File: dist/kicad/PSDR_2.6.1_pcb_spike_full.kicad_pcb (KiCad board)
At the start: 4 copper layers, 100 x 65 mm, 391 parts, among them J153 0.1in_6P_HEADER_DUAL_ENTRY_12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, J170 SPI_LCD_BOTTOM_ENTRY, M1 MH3M_PLATED, M2 MH3M_PLATED, M3 MH3M_PLATED, M4 MH3M, M5 MH3M, M6 MH3M, M7 MH3M, Q126 MOSFET_P_SOT23_IRLML6401, Q178 MOSFET_P_SOT23_IRLML6401, Q208 MOSFET_P_SOT23_IRLML6401, Q246 MOSFET_P_SOT23_IRLML6401, Q5 MOSFET_P_SOT23_IRLML6401, U114 BUCK_REGULATOR_AP3417C, U121 STM32F746_LQFP100, U131 OP_AMP_FAN4174, U15 DIGITAL_POT_MAX5388, U16 RF_DPDT_MASWSS0129TR, U161 BAT-MANAGE_MCP73871, U172 3V3_LDO_MCP1802, U18 DPDT_ANALOG_MAX4525, U185 GPS_MODULE_RXM-GPS-RM-T, U189 MIC_PREAMP_SSM2167, U199 AUDIO_AMP_TPA0253DGQR, U211 74CBTLV3253, U216 OP_AMP_FAN4174, U227 OP_AMP_FAN4174, U24 RF_DPDT_MASWSS0129TR, U241 SI5338, U253 AD8131, U255 MCP6N11, U260 AD8131, U272 MCP6N11, U279 SY10EP52V, U280 SY10EP52V, U287 VARIABLE_FILTER_HMC1023, U298 74CBTLV3253, U30 RF_DPDT_MASWSS0129TR, U304 MMIC-AMP_HMC482ST, U314 AD8302, U32 MICROPHONE_MEMS_SPU0410HR5H-PB, U37 SPDT_ANALOG_SWITCH_SN74LVC1G3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, U4 DPDT_ANALOG_MAX4525, U47 OP_AMP_FAN4174, U58 OP_AMP_FAN4174, U85 BOOST_REG_ADP1613, U86 DPDT_ANALOG_MAX4525, X1 MH_80M, X2 MH_80M, Y182 CRYSTAL3225, Y183 CRYSTAL_SMT_32.768, Y237 CRYSTAL3225

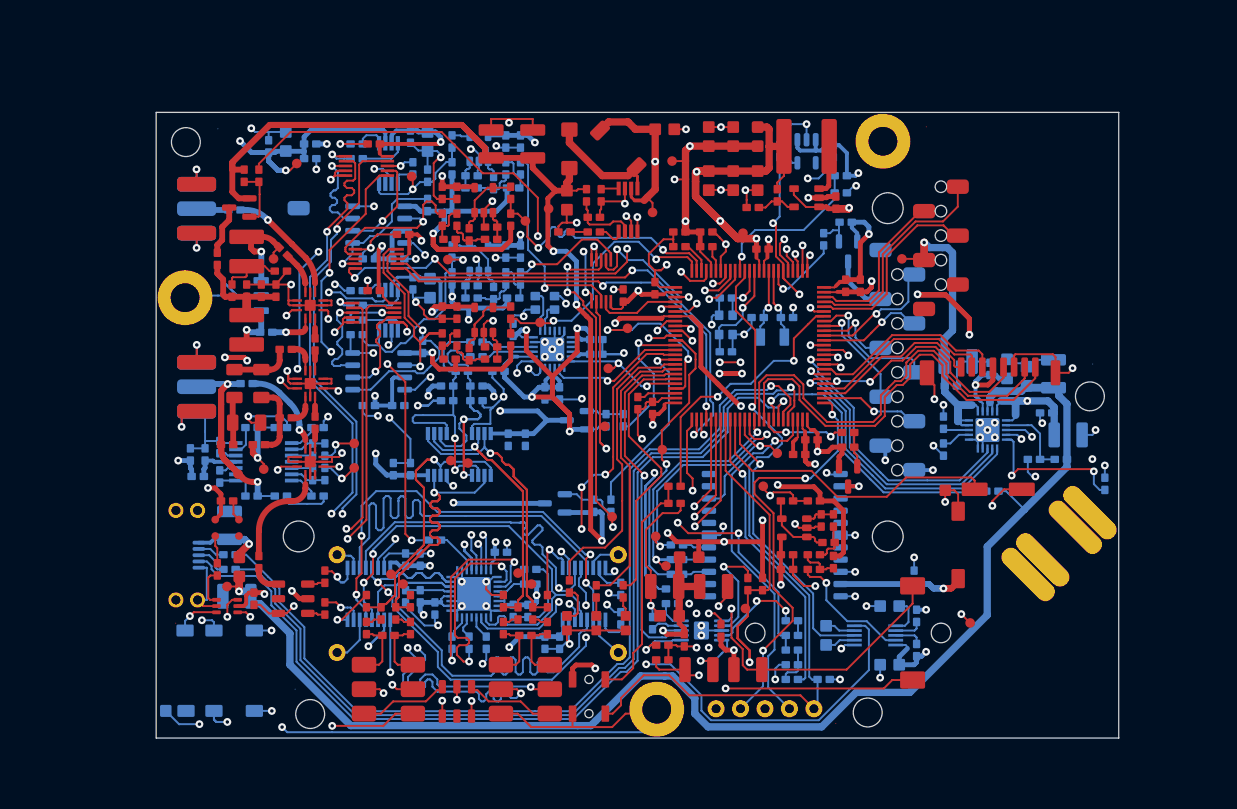
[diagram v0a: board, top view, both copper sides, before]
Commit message: feat(pcb): 补上铺铜、真实板框与丝印，四层板 0 断点
- 板框取 *LINES* 里唯一的 BOARD 记录：68 顶点 / 67 段（42 直线 + 25 弧），
  对 2.6.1 fabnotes 真弧采样 2144 点，最差 0.0025 mm。
- 铺铜取 *POUR* 的 12 个 POUROUT（7 个网），GND 连通性 20 → 0。
- 丝印取 decal 图元 + 板级 level 26/29 + 位号 + 自由文本；双向覆盖率
  2/8 mil 100%，10 mil 仅剩一处 9 笔画未定位的实心三角。
- 修 gerbparse 的 G75 整圆弧（start == end 被当零扫角）。
- DRC 795 条 / 0 断点，均为源设计允许的丝印压焊盘、紧间距与库缺失；
  生产包仍以上游 468dc41 的原始 Gerber 为准。
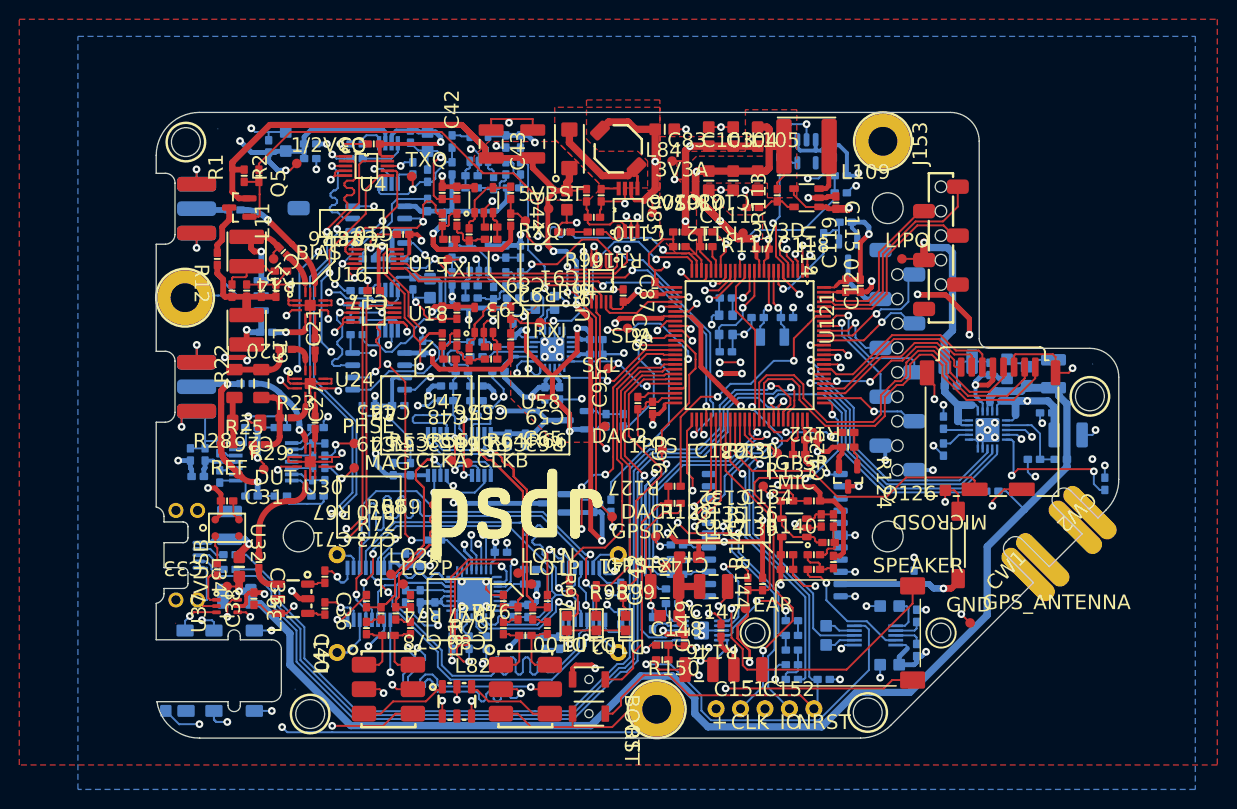
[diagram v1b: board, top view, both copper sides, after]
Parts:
- removed the C10 at (25.7, -52.3)
- removed the C119 at (71.6, -47.0)
- removed the C13 at (13.2, -50.5)
- removed the C139 at (68.3, -17.5)
- removed the C152 at (61.5, -7.11)
- removed the C158 at (83.3, -39.1)
- removed the C179 at (59.2, -45.7)
- removed the C197 at (66.0, -7.62)
- removed the C21 at (16.5, -40.9)
- removed the C215 at (36.3, -62.0)
- removed the C235 at (35.1, -46.2)
- removed the C243 at (40.4, -35.8)
- removed the C256 at (25.1, -49.8)
- removed the C262 at (20.8, -45.0)
- removed the C27 at (16.5, -32.8)
- removed the C289 at (25.9, -18.5)
- removed the C294 at (30.7, -9.91)
- removed the C303 at (8.13, -54.9)
- removed the C31 at (7.37, -24.6)
- removed the C320 at (16.8, -25.1)
- removed the C38 at (10.2, -14.5)
- removed the C46 at (31.2, -44.2)
- removed the C89 at (42.7, -55.9)
- removed the CLK at (60.7, -3.05)
- removed the J153 at (81.5, -50.9)
- removed the L34 at (8.64, -17.8)
- removed the L84 at (48.0, -61.2)
- removed the LO1N at (37.6, -17.1)
- removed the MIC at (63.1, -26.2)
- removed the R112 at (62.0, -55.1)
- removed the R122 at (71.9, -31.8)
- removed the R133 at (70.4, -22.6)
- removed the R165 at (91.2, -29.0)
- removed the R175 at (71.1, -56.6)
- removed the R194 at (66.0, -12.2)
- removed the R201 at (54.1, -18.5)
- removed the R206 at (47.2, -24.1)
- removed the R274 at (30.2, -35.1)
- removed the R300 at (16.0, -60.2)
- removed the R6 at (7.87, -46.5)
- removed the R74 at (36.1, -14.2)
- added C120: CAP_0603, PSDR:CAP_0603, F.Cu at (73.2, -47.0)
- added C134: CAP_0603, PSDR:CAP_0603, F.Cu at (69.8, -20.3)
- added C155: CSM-X5R-10U0-10P-25V-0805, PSDR:CSM-X5R-10U0-10P-25V-0805, B.Cu at (90.4, -37.6)
- added C173: CAP_0603, PSDR:CAP_0603, B.Cu at (64.8, -61.0)
- added C191: CSM-X5R-10U0-10P-25V-0805, PSDR:CSM-X5R-10U0-10P-25V-0805, B.Cu at (76.2, -7.62)
- added C205: CAP_0603, PSDR:CAP_0603, B.Cu at (51.6, -11.9)
- added C214: CAP_0603, PSDR:CAP_0603, B.Cu at (37.8, -62.0)
- added C238: CAP_0603, PSDR:CAP_0603, B.Cu at (45.7, -41.4)
- added C248: CAP_0603, PSDR:CAP_0603, B.Cu at (26.4, -62.5)
- added C259: CAP_0603, PSDR:CAP_0603, B.Cu at (26.7, -47.2)
- added C269: CAP_0603, PSDR:CAP_0603, B.Cu at (35.6, -38.1)
- added C290: CAP_0603, PSDR:CAP_0603, B.Cu at (38.6, -13.2)
- added C3: CAP_0603, PSDR:CAP_0603, F.Cu at (22.6, -61.7)
- added C307: CAP_0603, PSDR:CAP_0603, B.Cu at (16.8, -32.3)
- added C318: CAP_0603, PSDR:CAP_0603, B.Cu at (6.60, -27.2)
- added C35: CAP_0603, PSDR:CAP_0603, F.Cu at (10.7, -18.3)
- added C45: CAP_0603, PSDR:CAP_0603, F.Cu at (29.7, -44.2)
- added C56: CAP_0603, PSDR:CAP_0603, F.Cu at (29.7, -56.6)
- added C7: CAP_0603, PSDR:CAP_0603, F.Cu at (9.40, -46.5)
- added C96: CAP_0603, PSDR:CAP_0603, F.Cu at (51.6, -34.3)
- added D101: LED_0603, PSDR:LED_0603, F.Cu at (45.7, -11.9)
- added IO: 0.1in_1PIN, PSDR:0.1in_1PIN, F.Cu at (65.8, -3.05)
- added J170: SPI_LCD_BOTTOM_ENTRY, PSDR:SPI_LCD_BOTTOM_ENTRY, B.Cu at (77.0, -38.0)
- added R1: RES_0603, PSDR:RES_0603, F.Cu at (9.14, -58.4)
- added R164: RES_0603, PSDR:RES_0603, B.Cu at (94.0, -29.0)
- added R2: RES_0603, PSDR:RES_0603, F.Cu at (10.7, -58.4)
- added R202: RES_0603, PSDR:RES_0603, B.Cu at (54.1, -17.0)
- added R232: RES_0603, PSDR:RES_0603, B.Cu at (30.7, -47.8)
- added R28: RES_0603, PSDR:RES_0603, F.Cu at (7.37, -30.5)
- added R299: RES_0603, PSDR:RES_0603, B.Cu at (16.0, -61.7)
- added R313: RES_0603, PSDR:RES_0603, B.Cu at (16.3, -27.4)
- added R52: RES_0603, PSDR:RES_0603, F.Cu at (36.8, -41.4)
- added R64: RES_0603, PSDR:RES_0603, F.Cu at (30.5, -51.8)
- added R72: RES_0603, PSDR:RES_0603, F.Cu at (24.1, -10.7)
- added R90: RES_0603, PSDR:RES_0603, F.Cu at (44.7, -56.4)
- added SCL: PAD_1MM, PSDR:PAD_1MM, F.Cu at (47.0, -38.4)
- added U16: RF_DPDT_MASWSS0129TR, PSDR:RF_DPDT_MASWSS0129TR, F.Cu at (16.0, -45.0)
- added U18: DPDT_ANALOG_MAX4525, PSDR:DPDT_ANALOG_MAX4525, F.Cu at (22.6, -44.2)
- added U216: OP_AMP_FAN4174, PSDR:OP_AMP_FAN4174, B.Cu at (33.5, -61.2)
- added U253: AD8131, PSDR:AD8131, B.Cu at (24.1, -59.7)
- added U287: VARIABLE_FILTER_HMC1023, PSDR:VARIABLE_FILTER_HMC1023, B.Cu at (33.0, -15.0)
- C10: renamed from C108; value CAP_0805 -> CAP_0603; footprint PSDR:CAP_0805 -> PSDR:CAP_0603
- C108: renamed from C120; value CAP_0603 -> CAP_0805; footprint PSDR:CAP_0603 -> PSDR:CAP_0805
- C13: renamed from C147; value CSM-X5R-10U0-10P-25V-0805 -> CAP_0603; footprint PSDR:CSM-X5R-10U0-10P-25V-0805 -> PSDR:CAP_0603
- C139: renamed from C155; value CSM-X5R-10U0-10P-25V-0805 -> CAP_0603; footprint PSDR:CSM-X5R-10U0-10P-25V-0805 -> PSDR:CAP_0603; moved to F.Cu
- C147: renamed from C159; value CAP_0603 -> CSM-X5R-10U0-10P-25V-0805; footprint PSDR:CAP_0603 -> PSDR:CSM-X5R-10U0-10P-25V-0805; moved to F.Cu
- C152: renamed from C173; value CAP_0603 -> CSM-X5R-22U-20P-10V-1210; footprint PSDR:CAP_0603 -> PSDR:CSM-X5R-22U-20P-10V-1210; moved to F.Cu
- C158: renamed from C188; value CSM-X5R-10U0-10P-25V-0805 -> CSM-X5R-22U-20P-10V-1210; footprint PSDR:CSM-X5R-10U0-10P-25V-0805 -> PSDR:CSM-X5R-22U-20P-10V-1210
- C159: renamed from C191; value CSM-X5R-10U0-10P-25V-0805 -> CAP_0603; footprint PSDR:CSM-X5R-10U0-10P-25V-0805 -> PSDR:CAP_0603
- C188: renamed from C214; value CAP_0603 -> CSM-X5R-10U0-10P-25V-0805; footprint PSDR:CAP_0603 -> PSDR:CSM-X5R-10U0-10P-25V-0805
- C21: renamed from C238; moved to F.Cu
- C262: renamed from C3; moved to B.Cu
- C27: renamed from C307; moved to F.Cu
- C289: renamed from C35; moved to B.Cu
- C294: renamed from C45; moved to B.Cu
- C303: renamed from C56; moved to B.Cu
- C320: renamed from C83; value CSM-X5R-10U0-10P-10V-0805 -> CAP_0603; footprint PSDR:CSM-X5R-10U0-10P-10V-0805 -> PSDR:CAP_0603; moved to B.Cu
- C46: renamed from D101; value LED_0603 -> CAP_0603; footprint PSDR:LED_0603 -> PSDR:CAP_0603
- C83: renamed from IO; value 0.1in_1PIN -> CSM-X5R-10U0-10P-10V-0805; footprint PSDR:0.1in_1PIN -> PSDR:CSM-X5R-10U0-10P-10V-0805
- C89: renamed from J170; value SPI_LCD_BOTTOM_ENTRY -> CAP_0805; footprint PSDR:SPI_LCD_BOTTOM_ENTRY -> PSDR:CAP_0805; moved to F.Cu
- CLK: renamed from L11; value IND_SMT_220UH_SRN4018-221M -> 0.1in_1PIN; footprint PSDR:IND_SMT_220UH_SRN4018-221M -> PSDR:0.1in_1PIN
- J153: renamed from R1; value RES_0603 -> 0.1in_6P_HEADER_DUAL_ENTRY_1241152-6; footprint PSDR:RES_0603 -> PSDR:0.1in_6P_HEADER_DUAL_ENTRY_1241152-6
- L11: renamed from R145; value RES_0603 -> IND_SMT_220UH_SRN4018-221M; footprint PSDR:RES_0603 -> PSDR:IND_SMT_220UH_SRN4018-221M
- L34: renamed from R164; value RES_0603 -> ISM-0805-10U; footprint PSDR:RES_0603 -> PSDR:ISM-0805-10U; moved to F.Cu
- L84: renamed from R2; value RES_0603 -> IND_4.7UH_SMT_CDRH4D28CNP-4R7PC; footprint PSDR:RES_0603 -> PSDR:IND_4.7UH_SMT_CDRH4D28CNP-4R7PC
- LO1N: renamed from R202; value RES_0603 -> PAD_1MM; footprint PSDR:RES_0603 -> PSDR:PAD_1MM; moved to F.Cu
- MIC: renamed from R232; value RES_0603 -> PAD_1MM; footprint PSDR:RES_0603 -> PSDR:PAD_1MM; moved to F.Cu
- R122: renamed from R299; moved to F.Cu
- R133: renamed from R313; moved to F.Cu
- R165: renamed from R64; moved to B.Cu
- R175: renamed from R72; moved to B.Cu
- R194: renamed from R90; moved to B.Cu
- R201: renamed from REF; value PAD_1MM -> RES_0603; footprint PSDR:PAD_1MM -> PSDR:RES_0603; moved to B.Cu
- R206: renamed from SCL; value PAD_1MM -> RES_0603; footprint PSDR:PAD_1MM -> PSDR:RES_0603; moved to B.Cu
- R274: renamed from U16; value RF_DPDT_MASWSS0129TR -> RES_0603; footprint PSDR:RF_DPDT_MASWSS0129TR -> PSDR:RES_0603; moved to B.Cu
- R300: renamed from U18; value DPDT_ANALOG_MAX4525 -> RES_0603; footprint PSDR:DPDT_ANALOG_MAX4525 -> PSDR:RES_0603; moved to B.Cu
- R6: renamed from U216; value OP_AMP_FAN4174 -> RES_0603; footprint PSDR:OP_AMP_FAN4174 -> PSDR:RES_0603; moved to F.Cu
- R74: renamed from U253; value AD8131 -> RES_0603; footprint PSDR:AD8131 -> PSDR:RES_0603; moved to F.Cu
- REF: renamed from U287; value VARIABLE_FILTER_HMC1023 -> PAD_1MM; footprint PSDR:VARIABLE_FILTER_HMC1023 -> PSDR:PAD_1MM; moved to F.Cu
- moved L34 86.1 mm to (8.64, -17.8)
- moved J153 72.8 mm to (81.5, -50.9)
- moved CLK 69.9 mm to (60.7, -3.05)
- moved R175 65.7 mm to (71.1, -56.6)
- moved R165 64.9 mm to (91.2, -29.0)
- moved L11 63.8 mm to (9.40, -50.5)
- moved R122 63.4 mm to (71.9, -31.8)
- moved C188 61.6 mm to (76.2, -13.7)
- moved C83 61.6 mm to (52.8, -63.2)
- moved R112 59.9 mm to (62.0, -55.1)
- moved C13 55.2 mm to (13.2, -50.5)
- moved R133 54.3 mm to (70.4, -22.6)
- moved C152 53.9 mm to (61.5, -7.11)
- moved C320 52.5 mm to (16.8, -25.1)
- moved C197 51.4 mm to (66.0, -7.62)
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- renumbered C134 to C119, C205 to C179, C225 to C197, C248 to C215, C259 to C225, C269 to C235, C281 to C243, C290 to C256, C318 to C281, C7 to C31, C96 to C38, R28 to R112, R52 to R145
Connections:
- C119 pad 1: $$$5711 -> +3V3_CPU
- C119 pad 2: $$$5476 -> GND
- C13 pad 1: GND -> $$$15374
- C13 pad 2: $$$14035 -> RF_AMP_IN
- C139 pad 1: GND -> MIC_AMP_OUT
- C139 pad 2: +5V -> $$$5312
- C147 pad 1: LIPO -> GND
- C147 pad 2: GND -> $$$14035
- C152 pad 1: VBAT_BKP -> $$$10136
- C152 pad 2: GND -> $$$9819
- C158 pad 1: $$$1679 -> LIPO
- C159 pad 1: +3V3 -> LIPO
- C179 pad 1: $$$10468 -> GND
- C179 pad 2: GND -> $$$23762
- C188 pad 1: +3V3 -> $$$1679
- C197 pad 1: +3V3 -> $$$2987
- C21 pad 1: +3V3_CPU -> $$$15380
- C21 pad 2: GND -> $$$16059
- C235 pad 1: +3V3_CPU -> $$$28430
- C235 pad 2: GND -> $$$28429
- C243 pad 1: +3V3_FLIP_FLOP -> +3V3_CPU
- C256 pad 1: LPF_5V -> +3V3
- C262 pad 1: +3V3 -> TX-I_DRIVER_P
- C262 pad 2: GND -> $$$15845
- C27 pad 1: $$$2472 -> $$$16065
- C27 pad 2: GND -> $$$17006
- C281 pad 1: GND -> +3V3_FLIP_FLOP
- C281 pad 2: $$$1694 -> GND
- C289 pad 1: $$$16013 -> +3V3
- C289 pad 2: $$$16999 -> GND
- C294 pad 1: +3V3 -> $$$31750
- C294 pad 2: GND -> $$$31748
- C303 pad 1: +3V3 -> $$$22336
- C303 pad 2: GND -> $$$15375
- C31 pad 1: GND -> +3V3
- C31 pad 2: +5V_AMP -> GND
- C320 pad 1: V_SUPPLY -> GND
- C320 pad 2: GND -> $$$2458
- C38 pad 1: +3V3_CPU -> +3V3
- C46 pad 1: $$$10534 -> +3V3
- C83 pad 1: JTMS/SWDIO -> V_SUPPLY
- C89 pad 1: +3V3_CPU -> +5V_BOOST
- CLK pad 1: RF_AMP_IN -> JTCK/SWCLK
- J153 pad 1: +5V_BOOST -> ENC_B
- J153 pad 2: $$$4060 -> ENC_A
- L11 pad 1: +3V3_CPU -> RF_AMP_IN
- L11 pad 2: EARPHONE_INSERTED -> $$$31361
- L34 pad 1: $$$16399 -> +5V
- L34 pad 2: +5V -> $$$12053
- L84 pad 1: AMP_POWER -> V_SUPPLY
- L84 pad 2: $$$4060 -> BOOST_LOOP
- LO1N pad 1: $$$21746 -> $$$5934
- MIC pad 1: TX-I_FILTERED -> MIC_FILTER_OUT
- R112 pad 1: RF_REF -> $$$24763
- R112 pad 2: $$$598 -> GND
- R122 pad 1: HALF_VCC -> $$$484
- R122 pad 2: +3V3 -> GPS_POWER
- R133 pad 1: $$$2891 -> $$$5476
- R133 pad 2: $$$596 -> $$$5502
- R145 pad 1: RX-I_FILTERED -> +3V3_CPU
- R145 pad 2: HALF_VCC -> EARPHONE_INSERTED
- R165 pad 1: $$$28428 -> GND
- R165 pad 2: HALF_VCC -> $$$16399
- R175 pad 1: MIXER_LO2N -> GND
- R175 pad 2: MIXER_LO2P -> LIPO_V
- R194 pad 1: $$$14589 -> $$$9712
- R194 pad 2: +5V_BOOST -> $$$9652
- R201 pad 1: RF_REF -> $$$21776
- R206 pad 1: I2C_SCL -> $$$9133
- R274 pad 2: GND -> $$$31408
- R300 pad 1: TX-I_DRIVER_P -> GND
- R300 pad 2: $$$9489 -> HALF_VCC
- R6 pad 1: $$$28433 -> $$$31361
- R6 pad 2: GND -> +5V_AMP
- R74 pad 1: $$$11912 -> GND
- R74 pad 2: HALF_VCC -> $$$5934
- REF pad 1: GND -> RF_REF
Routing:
- added copper zone on F.Cu, net +3V3
- added copper zone on In1.Cu, net +3V3
- added copper zone on F.Cu, net +3V3_CPU
- added copper zone on In1.Cu, net +3V3_CPU
- added copper zone on In1.Cu, net +3V3_FLIP_FLOP
- added copper zone on F.Cu, net +5V_BOOST
- added copper zone on F.Cu, net BOOST_LOOP
- added copper zone on B.Cu, net GND
- added copper zone on F.Cu, net GND
- added copper zone on In2.Cu, net GND
- added copper zone on F.Cu, net V_SUPPLY
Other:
- outline, holes or cut-outs redrawn
- board text added: "+"
- board text added: "-"
- board text added: "1/2VCC"
- board text added: "1PPS"
- board text added: "3V3A"
- board text added: "3V3D"
- board text added: "5VBST"
- board text added: "ANT/VNA-IN"
- board text added: "BIAS"
- board text added: "BOOT"
- board text added: "C10"
- board text added: "C103"
- board text added: "C104"
- board text added: "C106"
- board text added: "C107"
- board text added: "C108"
- board text added: "C110"
- board text added: "C111"
- board text added: "C115"
- board text added: "C118"
- board text added: "C119"
- board text added: "C120"
- board text added: "C123"
- board text added: "C125"
- board text added: "C129"
- board text added: "C13"
- board text added: "C132"
- board text added: "C134"
- board text added: "C135"
- board text added: "C137"
- board text added: "C139"
- board text added: "C142"
- board text added: "C143"
- board text added: "C147"
- board text added: "C148"
- board text added: "C149"
- board text added: "C151"
- board text added: "C152"
- board text added: "C154"
- board text added: "C155"
- board text added: "C156"
- board text added: "C157"
- board text added: "C158"
- board text added: "C159"
- board text added: "C160"
- board text added: "C163"
- board text added: "C17"
- board text added: "C171"
- board text added: "C173"
- board text added: "C179"
- board text added: "C180"
- board text added: "C181"
- board text added: "C184"
- board text added: "C186"
- board text added: "C188"
- board text added: "C191"
- board text added: "C192"
- board text added: "C193"
- board text added: "C195"
- board text added: "C197"
- board text added: "C20"
- board text added: "C203"
- board text added: "C205"
- board text added: "C209"
- board text added: "C21"
- board text added: "C210"
- board text added: "C212"
- board text added: "C213"
- board text added: "C214"
- board text added: "C215"
- board text added: "C217"
- board text added: "C218"
- board text added: "C220"
- board text added: "C223"
- board text added: "C225"
- board text added: "C226"
- board text added: "C228"
- board text added: "C229"
- board text added: "C231"
- board text added: "C235"
- board text added: "C238"
- board text added: "C239"
- board text added: "C240"
- board text added: "C242"
- board text added: "C243"
- board text added: "C247"
- board text added: "C248"
- board text added: "C251"
- board text added: "C252"
- board text added: "C256"
- board text added: "C257"
- board text added: "C258"
- board text added: "C259"
- board text added: "C26"
- board text added: "C262"
- board text added: "C263"
- board text added: "C265"
- board text added: "C267"
- board text added: "C269"
- board text added: "C27"
- board text added: "C275"
- board text added: "C276"
- board text added: "C277"
- board text added: "C278"
- board text added: "C281"
- board text added: "C282"
- board text added: "C283"
- board text added: "C284"
- board text added: "C288"
- board text added: "C289"
- board text added: "C290"
- board text added: "C291"
- board text added: "C292"
- board text added: "C293"
- board text added: "C294"
- board text added: "C295"
- board text added: "C3"
- board text added: "C301"
- board text added: "C302"
- board text added: "C303"
- board text added: "C305"
- board text added: "C306"
- board text added: "C307"
- board text added: "C309"
- board text added: "C31"
- board text added: "C315"
- board text added: "C316"
- board text added: "C317"
- board text added: "C318"
- board text added: "C320"
- board text added: "C322"
- board text added: "C323"
- board text added: "C326"
- board text added: "C33"
- board text added: "C35"
- board text added: "C36"
- board text added: "C38"
- board text added: "C40"
- board text added: "C42"
- board text added: "C43"
- board text added: "C45"
- board text added: "C46"
- board text added: "C48"
- board text added: "C49"
- board text added: "C51"
- board text added: "C54"
- board text added: "C56"
- board text added: "C57"
- board text added: "C59"
- board text added: "C60"
- board text added: "C62"
- board text added: "C65"
- board text added: "C7"
- board text added: "C71"
- board text added: "C73"
- board text added: "C78"
- board text added: "C8"
- board text added: "C80"
- board text added: "C83"
- board text added: "C87"
- board text added: "C88"
- board text added: "C89"
- board text added: "C9"
- board text added: "C91"
- board text added: "C93"
- board text added: "C95"
- board text added: "C96"
- board text added: "CLK"
- board text added: "CLKA"
- board text added: "CLKB"
- board text added: "CW1"
- board text added: "CW2"
- board text added: "D100"
- board text added: "D101"
- board text added: "D102"
- board text added: "D44"
- board text added: "DAC1"
- board text added: "DAC2"
- board text added: "DUT"
- board text added: "EAR"
- board text added: "EARPHONE"
- board text added: "E_FILT_IF_N"
- board text added: "E_FILT_IF_P"
- board text added: "E_FILT_RF_N"
- board text added: "E_FILT_RF_P"
- board text added: "GND"
- board text added: "GPSR"
- board text added: "GPSRX"
- board text added: "GPSTX"
- board text added: "GPS_ANTENNA"
- board text added: "HW V2.6.1 - 6/29/2016"
- board text added: "IO"
- board text added: "J153"
- board text added: "J170"
- board text added: "L105"
- board text added: "L109"
- board text added: "L11"
- board text added: "L141"
- board text added: "L19"
- board text added: "L34"
- board text added: "L39"
- board text added: "L41"
- board text added: "L81"
- board text added: "L82"
- board text added: "L84"
- board text added: "LIPO"
- board text added: "LO1N"
- board text added: "LO1P"
- board text added: "LO2N"
- board text added: "LO2P"
- board text added: "MAG"
- board text added: "MIC"
- board text added: "MICROSD"
- board text added: "Michael Colton - KE7HIA"
- board text added: "NRST"
- board text added: "PHSE"
- board text added: "Q126"
- board text added: "Q178"
- board text added: "Q208"
- board text added: "Q246"
- board text added: "Q5"
- board text added: "R1"
- board text added: "R112"
- board text added: "R113"
- board text added: "R116"
- board text added: "R117"
- board text added: "R12"
- board text added: "R122"
- board text added: "R124"
- board text added: "R127"
- board text added: "R128"
- board text added: "R130"
- board text added: "R133"
- board text added: "R136"
- board text added: "R14"
- board text added: "R140"
- board text added: "R144"
- board text added: "R145"
- board text added: "R146"
- board text added: "R150"
- board text added: "R162"
- board text added: "R164"
- board text added: "R165"
- board text added: "R167"
- board text added: "R168"
- board text added: "R169"
- board text added: "R174"
- board text added: "R175"
- board text added: "R176"
- board text added: "R177"
- board text added: "R187"
- board text added: "R190"
- board text added: "R194"
- board text added: "R196"
- board text added: "R198"
- board text added: "R2"
- board text added: "R200"
- board text added: "R201"
- board text added: "R202"
- board text added: "R204"
- board text added: "R206"
- board text added: "R207"
- board text added: "R219"
- board text added: "R22"
- board text added: "R221"
- board text added: "R222"
- board text added: "R224"
- board text added: "R23"
- board text added: "R230"
- board text added: "R232"
- board text added: "R234"
- board text added: "R236"
- board text added: "R244"
- board text added: "R245"
- board text added: "R249"
- board text added: "R25"
- board text added: "R250"
- board text added: "R254"
- board text added: "R261"
- board text added: "R264"
- board text added: "R266"
- board text added: "R268"
- board text added: "R270"
- board text added: "R271"
- board text added: "R273"
- board text added: "R274"
- board text added: "R28"
- board text added: "R285"
- board text added: "R286"
- board text added: "R29"
- board text added: "R296"
- board text added: "R297"
- board text added: "R299"
- board text added: "R300"
- board text added: "R308"
- board text added: "R310"
- board text added: "R311"
- board text added: "R312"
- board text added: "R313"
- board text added: "R319"
- board text added: "R321"
- board text added: "R324"
- board text added: "R325"
- board text added: "R50"
- board text added: "R52"
- board text added: "R53"
- board text added: "R55"
- board text added: "R6"
- board text added: "R61"
- board text added: "R63"
- board text added: "R64"
- board text added: "R66"
- board text added: "R67"
- board text added: "R68"
- board text added: "R69"
- board text added: "R70"
- board text added: "R72"
- board text added: "R74"
- board text added: "R75"
- board text added: "R76"
- board text added: "R77"
- board text added: "R79"
- board text added: "R90"
- board text added: "R92"
- board text added: "R94"
- board text added: "R97"
- board text added: "R98"
- board text added: "R99"
- board text added: "REF"
- board text added: "RST"
- board text added: "RXI"
- board text added: "RXQ"
- board text added: "SCL"
- board text added: "SDA"
- board text added: "SPEAKER"
- board text added: "Serial No"
- board text added: "TXI"
- board text added: "TXQ"
- board text added: "U114"
- board text added: "U121"
- board text added: "U131"
- board text added: "U15"
- board text added: "U16"
- board text added: "U161"
- board text added: "U172"
- board text added: "U18"
- board text added: "U185"
- board text added: "U189"
- board text added: "U199"
- board text added: "U211"
- board text added: "U216"
- board text added: "U227"
- board text added: "U24"
- board text added: "U241"
- board text added: "U253"
- board text added: "U255"
- board text added: "U260"
- board text added: "U272"
- board text added: "U279"
- board text added: "U280"
- board text added: "U287"
- board text added: "U298"
- board text added: "U30"
- board text added: "U304"
- board text added: "U314"
- board text added: "U32"
- board text added: "U37"
- board text added: "U4"
- board text added: "U47"
- board text added: "U58"
- board text added: "U85"
- board text added: "U86"
- board text added: "USB"
- board text added: "VNA-OUT"
- board text added: "VSPLY"
- board text added: "VUSB"
- board text added: "Y182"
- board text added: "Y183"
- board text added: "Y237"
- board text added: "portablesdr.com"
